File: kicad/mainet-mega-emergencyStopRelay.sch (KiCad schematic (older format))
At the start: 38 parts, among them J38 Screw_Terminal_01x01, J39 Screw_Terminal_01x01, J41 Screw_Terminal_01x01, J43 Screw_Terminal_01x01, J45 Screw_Terminal_01x01, J46 Screw_Terminal_01x01, J47 Screw_Terminal_01x01, J48 Screw_Terminal_01x01, J49 Screw_Terminal_01x01, J50 Screw_Terminal_01x01, J51 Screw_Terminal_01x01, J52 Screw_Terminal_01x01, J53 Screw_Terminal_01x01, J54 Screw_Terminal_01x01, J55 Screw_Terminal_01x01, J56 Screw_Terminal_01x01, J57 Screw_Terminal_01x01, J58 Screw_Terminal_01x01, J59 Screw_Terminal_01x01, J60 Screw_Terminal_01x01, J61 Screw_Terminal_01x01, J62 Screw_Terminal_01x01, J63 Screw_Terminal_01x01, K10 Contactor-3-poles, K9 relay-4p2t, SW5 emergencyStop, T1 Transformer_2P_1S, U11 socket-4p2t

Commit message: KICAD: Actualizar archivos sch
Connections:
- net labels added: GNDREF
- net labels removed: GNDA
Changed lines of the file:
@@
-$EndComp
-$Comp
-L power:GNDA #PWR039
-U 1 1 5FDC5B2D
-P 750 7300
-F 0 "#PWR039" H 750 7050 50  0001 C CNN
-F 1 "GNDA" H 755 7127 50  0000 C CNN
-F 2 "" H 750 7300 50  0001 C CNN
-F 3 "" H 750 7300 50  0001 C CNN
-	1    750  7300
-	1    0    0    -1
-$EndComp
-$Comp
-L power:PWR_FLAG #FLG05
-U 1 1 5FDC5C70
-P 3450 5300
-F 0 "#FLG05" H 3450 5375 50  0001 C CNN
-F 1 "PWR_FLAG" H 3450 5473 50  0000 C CNN
-F 2 "" H 3450 5300 50  0001 C CNN
-F 3 "~" H 3450 5300 50  0001 C CNN
-	1    3450 5300
-	1    0    0    -1
 $EndComp
 $Comp
 L power:PWR_FLAG #FLG06
 U 1 1 5FDC5CFA
-P 1200 7300
-F 0 "#FLG06" H 1200 7375 50  0001 C CNN
-F 1 "PWR_FLAG" H 1200 7473 50  0000 C CNN
-F 2 "" H 1200 7300 50  0001 C CNN
-F 3 "~" H 1200 7300 50  0001 C CNN
-	1    1200 7300
+P 1550 6500
+F 0 "#FLG06" H 1550 6575 50  0001 C CNN
+F 1 "PWR_FLAG" H 1550 6673 50  0000 C CNN
+F 2 "" H 1550 6500 50  0001 C CNN
+F 3 "~" H 1550 6500 50  0001 C CNN
+	1    1550 6500
 	1    0    0    1
 $EndComp
 Wire Wire Line
-	750  7300 1200 7300
-$Comp
-L power:GNDA #PWR041
-U 1 1 5FDC9687
-P 1100 6500
-F 0 "#PWR041" H 1100 6250 50  0001 C CNN
-F 1 "GNDA" H 1105 6327 50  0000 C CNN
-F 2 "" H 1100 6500 50  0001 C CNN
-F 3 "" H 1100 6500 50  0001 C CNN
-	1    1100 6500
-	1    0    0    -1
-$EndComp
+	1100 6500 1550 6500
 Wire Wire Line
 	1100 5300 1100 5700
@@
 Text Label 2850 1700 0    50   ~ 0
 L11
+$Comp
+L power:GNDREF #PWR0108
+U 1 1 60EEEDA8
+P 1100 6500
+F 0 "#PWR0108" H 1100 6250 50  0001 C CNN
+F 1 "GNDREF" H 1105 6327 50  0000 C CNN
+F 2 "" H 1100 6500 50  0001 C CNN
+F 3 "" H 1100 6500 50  0001 C CNN
+	1    1100 6500
+	1    0    0    -1
+$EndComp
+Connection ~ 1100 6500
+$Comp
+L power:PWR_FLAG #FLG0102
+U 1 1 60F2B4A9
+P 3450 5300
+F 0 "#FLG0102" H 3450 5375 50  0001 C CNN
+F 1 "PWR_FLAG" H 3450 5473 50  0000 C CNN
+F 2 "" H 3450 5300 50  0001 C CNN
+F 3 "~" H 3450 5300 50  0001 C CNN
+	1    3450 5300
+	1    0    0    -1
+$EndComp
 $EndSCHEMATC

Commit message: KICAD: Actualizar .sch regleta de conexiones
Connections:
- net L5 is gone; now on net L4: F5.2, T1.3 (H3)
- net 5 renamed Neutro
- net L11 renamed 120VAC
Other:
- moved on the sheet: F14, F4, F5, F6, FU1, FU2, FU3, FU7, FU8, FU9, J38, J39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

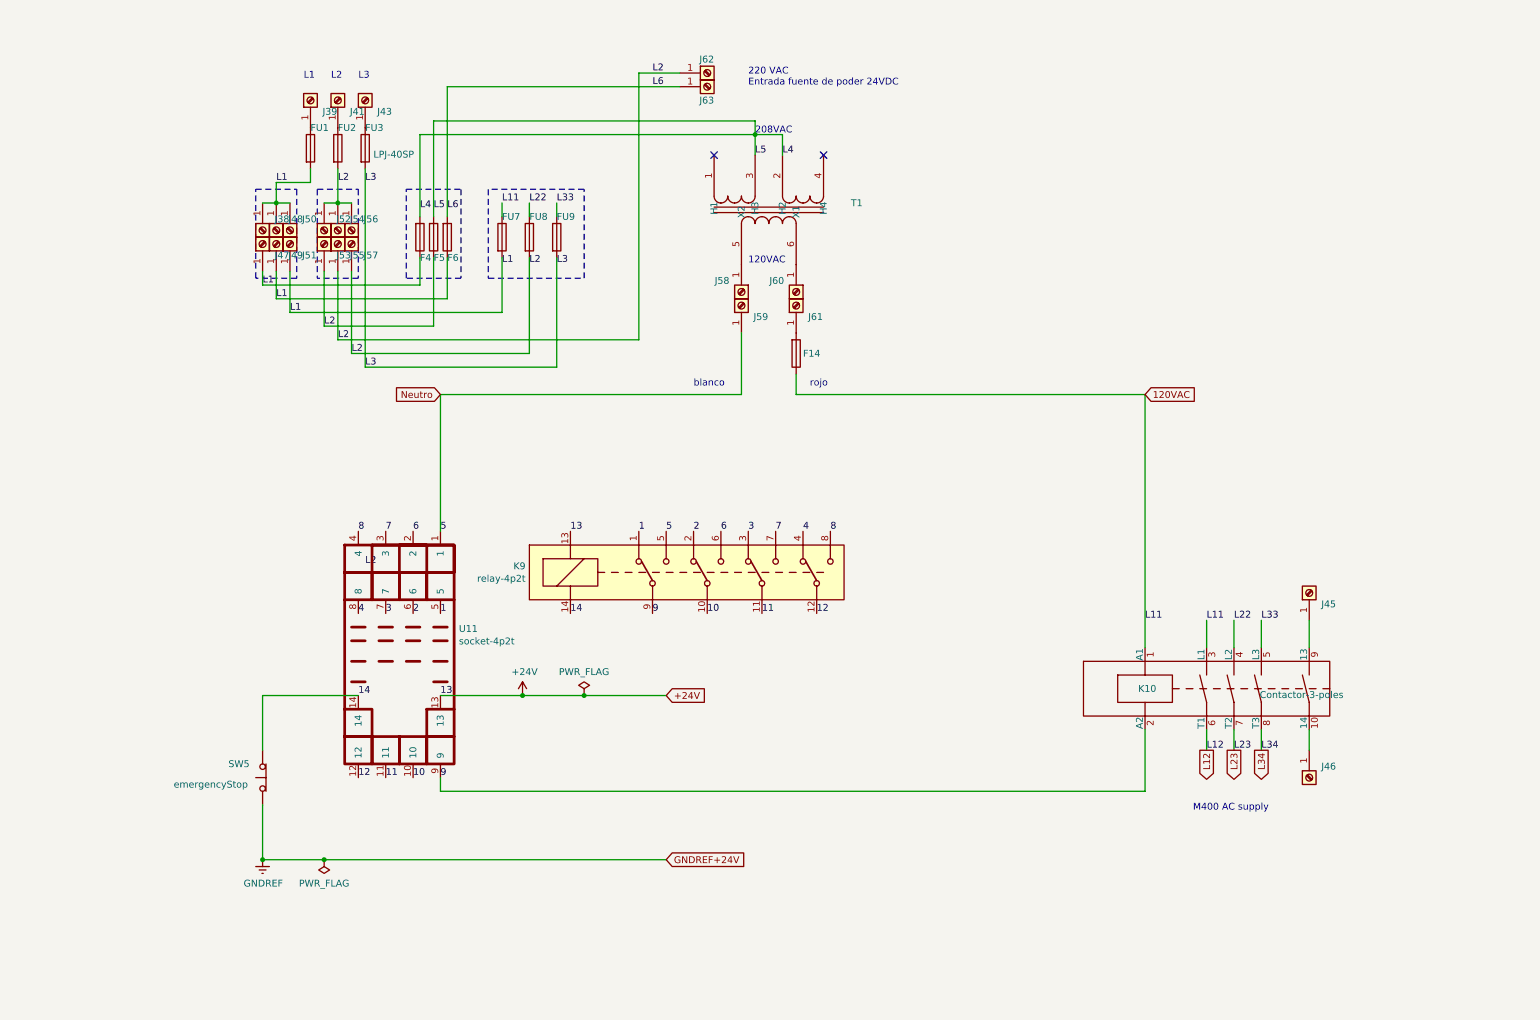
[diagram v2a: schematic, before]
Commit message: KICAD: Actualizar sch del pulsador de emergencia
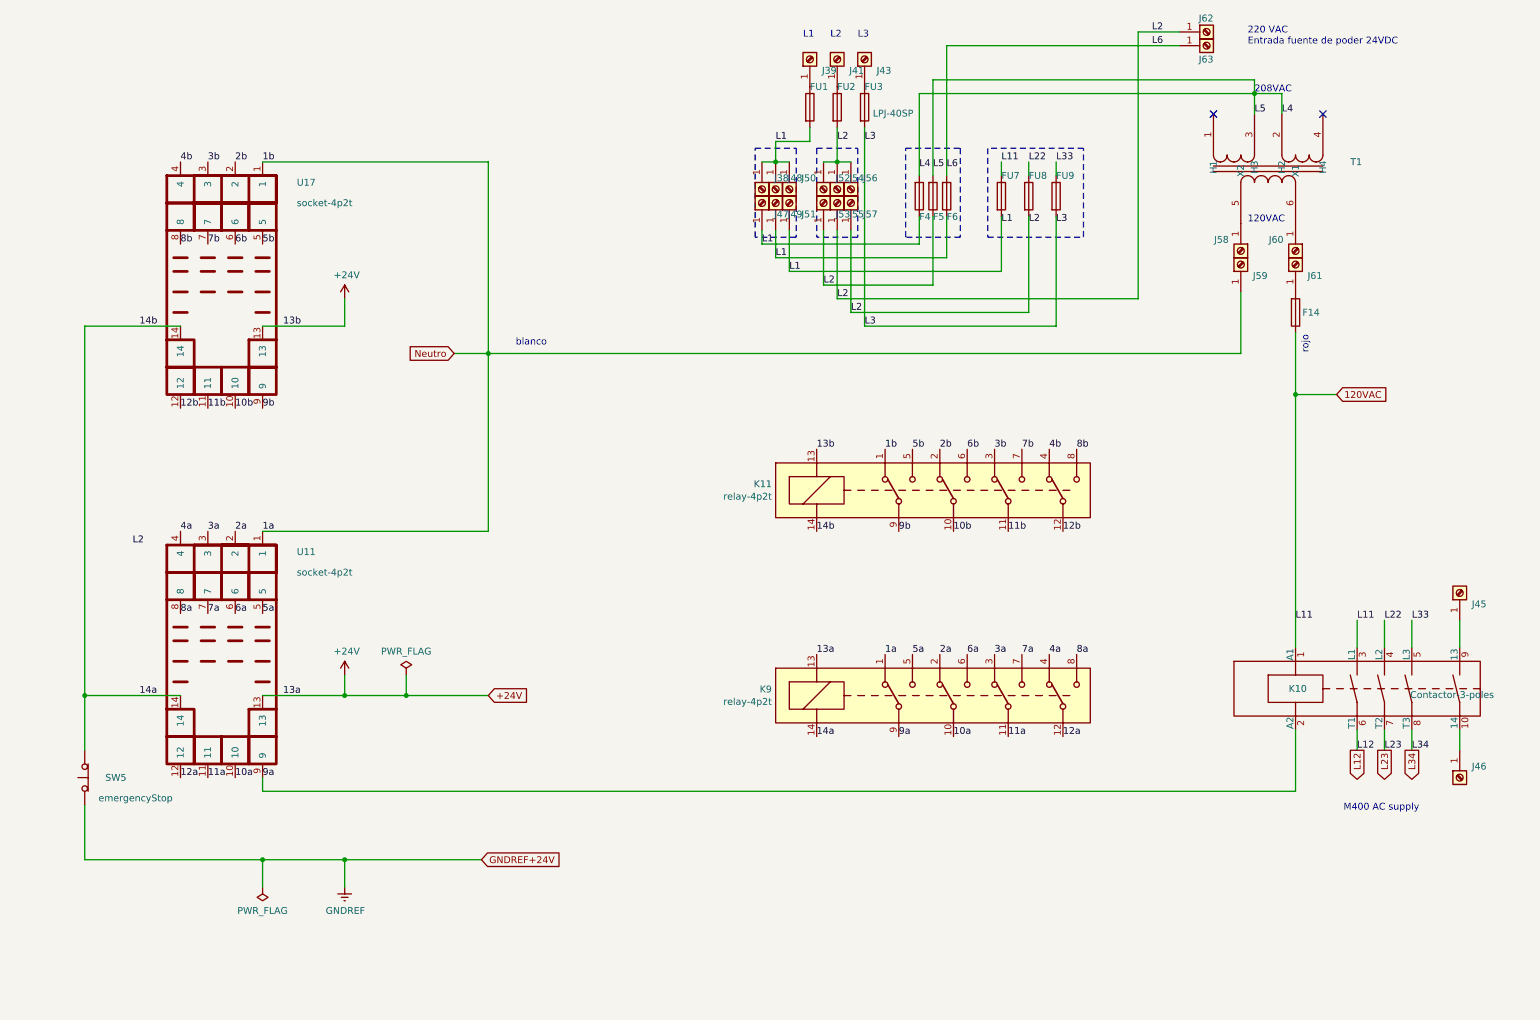
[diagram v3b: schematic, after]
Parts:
- added K11: relay-4p2t, symbol mainet-mega-rescue:relay-4p2t-ng-relays
- added U17: socket-4p2t, symbol mainet-mega-rescue:socket-4p2t-ng-relays
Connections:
- net +24V: now also K11.13 (+), U17.13
- net Neutro: now also K9.1 (NC1), K11.1 (NC1), U17.1; no longer K9.5 (NO1)
- net 1 renamed 5a
- net 5a: now also K9.5 (NO1); no longer K9.1 (NC1)
- net 10 renamed 10a
- net 11 renamed 11a
- net 12 renamed 12a
- net 14 renamed 14a
- net 14a: now also K11.14 (-), U17.14
- net 2 renamed 2a
- net 2a: now also U11.2; no longer U11.6
- net 3 renamed 3a
- net 3a: now also U11.3; no longer U11.7
- net 4 renamed 4a
- net 4a: now also U11.4; no longer U11.8
- net 6 renamed 6a
- net 6a: now also U11.6; no longer U11.2
- net 7 renamed 7a
- net 7a: now also U11.7; no longer U11.3
- net 8 renamed 8a
- net 8a: now also U11.8; no longer U11.4
- net 9 renamed 9a
- new net 10b: K11.10 (C2), U17.10
- new net 11b: K11.11 (C3), U17.11
- new net 12b: K11.12 (C4), U17.12
- new net 2b: K11.2 (NC2), U17.2
- new net 3b: K11.3 (NC3), U17.3
- new net 4b: K11.4 (NC4), U17.4
- new net 5b: K11.5 (NO1), U17.5
- new net 6b: K11.6, U17.6
- new net 7b: K11.7 (NO3), U17.7
- new net 8b: K11.8 (NO4), U17.8
- new net 9b: K11.9 (C1), U17.9
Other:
- moved on the sheet: F14, F4, F5, F6, FU1, FU2, FU3, FU7, FU8, FU9, J38, J39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

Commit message: KICAD: Actualizar .sch del relé de parada de emergencia
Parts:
- added J102: Screw_Terminal_01x02, symbol Connector:Screw_Terminal_01x02
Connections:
- net 10b: now also J102.2 (Pin_2)
- net 9b: now also J102.1 (Pin_1)
- net Neutro: no longer K11.1 (NC1), U17.1
- net 2b renamed lowerClutch2+
- net 3b renamed lowerClutch1-
- net 4b renamed lowerClutch1+
- new net lowerClutch2-: K11.1 (NC1), U17.1
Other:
- note added: "Ouput-"
- note added: "Output+"
- note added: "Tarjeta MP2"
- moved on the sheet: K11, K9, U17
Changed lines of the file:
@@
 Sheet 4 22
 Title "Mainet-mega -- Diagrama Alimentación AC"
-Date "2021-07-15"
+Date "2021-07-16"
 Rev "1.0"
 Comp "Tovenca"
@@
 L mainet-mega-rescue:relay-4p2t-ng-relays K9
 U 1 1 5FE04F1A
-P 6950 5600
+P 4200 4900
 AR Path="/5FE04F1A" Ref="K9"  Part="1"
 AR Path="/5FF9030A/5FE04F1A" Ref="K9"  Part="1"
-F 0 "K9" H 5722 5646 50  0000 R CNN
-F 1 "relay-4p2t" H 5722 5555 50  0000 R CNN
-F 2 "" H 7400 6500 50  0001 C CNN
-F 3 "" H 7400 6500 50  0001 C CNN
-	1    6950 5600
+F 0 "K9" H 2972 4946 50  0000 R CNN
+F 1 "relay-4p2t" H 2972 4855 50  0001 R CNN
+F 2 "" H 4650 5800 50  0001 C CNN
+F 3 "" H 4650 5800 50  0001 C CNN
+	1    4200 4900
 	1    0    0    -1
 $EndComp
@@
 	1    0    0    -1
 $EndComp
-Text Label 1050 4500 0    50   ~ 0
-L2
 Text Label 9550 5050 0    50   ~ 0
 L11
@@
 Wire Wire Line
 	10750 5850 10750 6000
-$Comp
-L mainet-mega-rescue:socket-4p2t-ng-relays U11
-U 1 1 5FDD58E8
-P 1700 5300
-AR Path="/5FDD58E8" Ref="U11"  Part="1"
-AR Path="/5FF9030A/5FDD58E8" Ref="U11"  Part="1"
-F 0 "U11" H 2250 6050 50  0000 L CNN
-F 1 "socket-4p2t" H 2250 5900 50  0000 L CNN
-F 2 "" H 2150 6200 50  0001 C CNN
-F 3 "" H 2150 6200 50  0001 C CNN
-	1    1700 5300
-	1    0    0    -1
-$EndComp
 Text Label 1400 4400 0    50   ~ 0
 4a
@@
 Text Label 2000 4400 0    50   ~ 0
 1a
-Text Label 7950 5300 0    50   ~ 0
+Text Label 5200 4600 0    50   ~ 0
 8a
-Text Label 6750 5300 0    50   ~ 0
+Text Label 4000 4600 0    50   ~ 0
 5a
-Text Label 7150 5300 0    50   ~ 0
+Text Label 4400 4600 0    50   ~ 0
 6a
-Text Label 7550 5300 0    50   ~ 0
+Text Label 4800 4600 0    50   ~ 0
 7a
 Text Label 1400 5000 0    50   ~ 0
@@
 Text Label 2150 5600 0    50   ~ 0
 13a
-Text Label 6950 5300 0    50   ~ 0
+Text Label 4200 4600 0    50   ~ 0
 2a
-Text Label 7350 5300 0    50   ~ 0
+Text Label 4600 4600 0    50   ~ 0
 3a
-Text Label 7750 5300 0    50   ~ 0
+Text Label 5000 4600 0    50   ~ 0
 4a
-Text Label 7050 5900 0    50   ~ 0
+Text Label 4300 5200 0    50   ~ 0
 10a
-Text Label 6650 5900 0    50   ~ 0
+Text Label 3900 5200 0    50   ~ 0
 9a
-Text Label 7450 5900 0    50   ~ 0
+Text Label 4700 5200 0    50   ~ 0
 11a
-Text Label 7850 5900 0    50   ~ 0
+Text Label 5100 5200 0    50   ~ 0
 12a
-Text Label 6550 5300 0    50   ~ 0
+Text Label 3800 4600 0    50   ~ 0
 1a
-Text Label 6050 5300 0    50   ~ 0
+Text Label 3300 4600 0    50   ~ 0
 13a
-Text Label 6050 5900 0    50   ~ 0
+Text Label 3300 5200 0    50   ~ 0
 14a
 Wire Wire Line
@@
 	0    -1   -1   0
 $EndComp
-Wire Wire Line
-	9150 2650 9150 3100
-Text Notes 3850 3050 0    50   ~ 0
+Text Notes 9100 3050 1    50   ~ 0
 blanco
 Text Notes 9650 3100 1    50   ~ 0
@@
 Text GLabel 9850 3400 2    50   Input ~ 0
 120VAC
-Text GLabel 3400 3100 0    50   Input ~ 0
+Text GLabel 8850 3400 0    50   Input ~ 0
 Neutro
 Connection ~ 9250 1200
@@
 L mainet-mega-rescue:socket-4p2t-ng-relays U?
 U 1 1 611478DC
-P 1700 2600
+P 1700 2050
 AR Path="/611478DC" Ref="U?"  Part="1"
 AR Path="/5FF9030A/611478DC" Ref="U17"  Part="1"
-F 0 "U17" H 2250 3350 50  0000 L CNN
-F 1 "socket-4p2t" H 2250 3200 50  0000 L CNN
-F 2 "" H 2150 3500 50  0001 C CNN
-F 3 "" H 2150 3500 50  0001 C CNN
-	1    1700 2600
-	1    0    0    -1
-$EndComp
-Wire Wire Line
-	700  5600 700  2900
-Wire Wire Line
-	700  2900 1400 2900
+F 0 "U17" H 900 2750 50  0000 L CNN
+F 1 "socket-4p2t" H 750 2650 50  0000 L CNN
+F 2 "" H 2150 2950 50  0001 C CNN
+F 3 "" H 2150 2950 50  0001 C CNN
+	1    1700 2050
+	1    0    0    -1
+$EndComp
+Wire Wire Line
+	700  2350 1400 2350
 Connection ~ 700  5600
 $Comp
 L mainet-mega-rescue:relay-4p2t-ng-relays K?
 U 1 1 611801A8
-P 6950 4100
+P 4200 2750
 AR Path="/611801A8" Ref="K?"  Part="1"
 AR Path="/5FF9030A/611801A8" Ref="K11"  Part="1"
-F 0 "K11" H 5722 4146 50  0000 R CNN
-F 1 "relay-4p2t" H 5722 4055 50  0000 R CNN
-F 2 "" H 7400 5000 50  0001 C CNN
-F 3 "" H 7400 5000 50  0001 C CNN
-	1    6950 4100
-	1    0    0    -1
-$EndComp
-Text Label 7950 3800 0    50   ~ 0
+F 0 "K11" H 2972 2796 50  0000 R CNN
+F 1 "relay-4p2t" H 2972 2705 50  0001 R CNN
+F 2 "" H 4650 3650 50  0001 C CNN
+F 3 "" H 4650 3650 50  0001 C CNN
+	1    4200 2750
+	1    0    0    -1
+$EndComp
+Text Label 5200 2450 0    50   ~ 0
 8b
-Text Label 6750 3800 0    50   ~ 0
+Text Label 4000 2450 0    50   ~ 0
 5b
-Text Label 7150 3800 0    50   ~ 0
+Text Label 4400 2450 0    50   ~ 0
 6b
-Text Label 7550 3800 0    50   ~ 0
+Text Label 4800 2450 0    50   ~ 0
 7b
-Text Label 6950 3800 0    50   ~ 0
+Text Label 4200 2450 0    50   ~ 0
 2b
-Text Label 7350 3800 0    50   ~ 0
+Text Label 4600 2450 0    50   ~ 0
 3b
-Text Label 7750 3800 0    50   ~ 0
+Text Label 5000 2450 0    50   ~ 0
 4b
-Text Label 7050 4400 0    50   ~ 0
+Text Label 4300 3050 0    50   ~ 0
 10b
-Text Label 6650 4400 0    50   ~ 0
+Text Label 3900 3050 0    50   ~ 0
 9b
-Text Label 7850 4400 0    50   ~ 0
+Text Label 5100 3050 0    50   ~ 0
 12b
-Text Label 6550 3800 0    50   ~ 0
+Text Label 3800 2450 0    50   ~ 0
 1b
-Text Label 6050 3800 0    50   ~ 0
+Text Label 3300 2450 0    50   ~ 0
 13b
-Text Label 6050 4400 0    50   ~ 0
+Text Label 3300 3050 0    50   ~ 0
 14b
 Wire Wire Line
-	9150 3100 3650 3100
-Wire Wire Line
-	3650 3100 3650 1700
-Wire Wire Line
-	3650 1700 2000 1700
-Wire Wire Line
-	2000 4400 3650 4400
-Connection ~ 3650 3100
-Wire Wire Line
-	3400 3100 3650 3100
-Wire Wire Line
 	2000 6300 9550 6300
-Wire Wire Line
-	3650 3100 3650 4400
 Wire Wire Line
 	2600 7000 2600 6800
@@
 	2000 6800 2600 6800
 Wire Wire Line
-	2000 2900 2600 2900
-Wire Wire Line
-	2600 2900 2600 2700
+	2000 2350 2600 2350
+Wire Wire Line
+	2600 2350 2600 2150
 $Comp
 L power:+24V #PWR050
 U 1 1 6120B21B
-P 2600 2700
-F 0 "#PWR050" H 2600 2550 50  0001 C CNN
-F 1 "+24V" H 2615 2873 50  0000 C CNN
-F 2 "" H 2600 2700 50  0001 C CNN
-F 3 "" H 2600 2700 50  0001 C CNN
-	1    2600 2700
+P 2600 2150
+F 0 "#PWR050" H 2600 2000 50  0001 C CNN
+F 1 "+24V" H 2615 2323 50  0000 C CNN
+F 2 "" H 2600 2150 50  0001 C CNN
+F 3 "" H 2600 2150 50  0001 C CNN
+	1    2600 2150
 	1    0    0    -1
 $EndComp
@@
 Wire Wire Line
 	3050 5450 3050 5600
-Text Label 7450 4400 0    50   ~ 0
+Text Label 4700 3050 0    50   ~ 0
 11b
-Text Label 2150 2900 0    50   ~ 0
+Text Label 2150 2350 0    50   ~ 0
 13b
-Text Label 1100 2900 0    50   ~ 0
+Text Label 1100 2350 0    50   ~ 0
 14b
-Text Label 2000 3500 0    50   ~ 0
+Text Label 2000 2950 0    50   ~ 0
 9b
-Text Label 1800 3500 0    50   ~ 0
+Text Label 1800 2950 0    50   ~ 0
 10b
-Text Label 1600 3500 0    50   ~ 0
+Text Label 1600 2950 0    50   ~ 0
 11b
-Text Label 1400 3500 0    50   ~ 0
+Text Label 1400 2950 0    50   ~ 0
 12b
-Text Label 1400 2300 0    50   ~ 0
+Text Label 1400 1750 0    50   ~ 0
 8b
-Text Label 1600 2300 0    50   ~ 0
+Text Label 1600 1750 0    50   ~ 0
 7b
-Text Label 1800 2300 0    50   ~ 0
+Text Label 1800 1750 0    50   ~ 0
 6b
-Text Label 2000 2300 0    50   ~ 0
+Text Label 2000 1750 0    50   ~ 0
 5b
-Text Label 1400 1700 0    50   ~ 0
+Text Label 1400 1150 0    50   ~ 0
 4b
-Text Label 1600 1700 0    50   ~ 0
+Text Label 1600 1150 0    50   ~ 0
 3b
-Text Label 1800 1700 0    50   ~ 0
+Text Label 1800 1150 0    50   ~ 0
 2b
-Text Label 2000 1700 0    50   ~ 0
+Text Label 2000 1150 0    50   ~ 0
 1b
+Text Notes 3700 3800 0    50   ~ 0
+Tarjeta MP2
+Wire Notes Line
+	3200 3400 4200 3400
+$Comp
+L Connector:Screw_Terminal_01x02 J?
+U 1 1 60F63F1D
+P 3150 3550
+AR Path="/60D1F41B/60F63F1D" Ref="J?"  Part="1"
+AR Path="/5FF9030A/60F63F1D" Ref="J102"  Part="1"
+F 0 "J102" H 3050 3700 50  0000 C CNN
+F 1 "Screw_Terminal_01x02" H 3068 3316 50  0001 C CNN
+F 2 "" H 3150 3550 50  0001 C CNN
+F 3 "~" H 3150 3550 50  0001 C CNN
+	1    3150 3550
+	1    0    0    -1
+$EndComp
+$Comp
+L mainet-mega-rescue:socket-4p2t-ng-relays U11
+U 1 1 5FDD58E8
+P 1700 5300
+AR Path="/5FDD58E8" Ref="U11"  Part="1"
+AR Path="/5FF9030A/5FDD58E8" Ref="U11"  Part="1"
+F 0 "U11" H 900 6000 50  0000 L CNN
+F 1 "socket-4p2t" H 750 5950 50  0000 L CNN
+F 2 "" H 2150 6200 50  0001 C CNN
+F 3 "" H 2150 6200 50  0001 C CNN
+	1    1700 5300
+	1    0    0    -1
+$EndComp
+Wire Wire Line
+	700  2350 700  5600
+Wire Wire Line
+	2000 4400 9150 4400
+Wire Wire Line
+	9150 2650 9150 3400
+Wire Wire Line
+	8850 3400 9150 3400
+Connection ~ 9150 3400
+Wire Wire Line
+	9150 3400 9150 4400
+Wire Notes Line
+	3200 3400 3200 3800
+Wire Notes Line
+	3200 3800 4200 3800
+Wire Notes Line
+	4200 3800 4200 3400
+Wire Wire Line
+	1800 2950 1800 3650
+Wire Wire Line
+	2000 2950 2000 3550
+Text Label 2050 3550 0    50   ~ 0
+lowerClutchControl-
+Text Label 2050 3650 0    50   ~ 0
+lowerClutchControl+
+Wire Wire Line
+	2000 3550 2950 3550
+Wire Wire Line
+	1800 3650 2950 3650
+Text Notes 3250 3550 0    50   ~ 0
+Ouput-
+Text Notes 3250 3700 0    50   ~ 0
+Output+
+Text GLabel 3000 650  2    50   Input ~ 0
+lowerClutch1+
+Text GLabel 3000 750  2    50   Input ~ 0
+lowerClutch1-
+Text GLabel 3000 850  2    50   Input ~ 0
+lowerClutch2+
+Text GLabel 3000 950  2    50   Input ~ 0
+lowerClutch2-
+Wire Wire Line
+	1400 650  3000 650
+Wire Wire Line
+	1400 650  1400 1150
+Wire Wire Line
+	3000 750  1600 750
+Wire Wire Line
+	1600 750  1600 1150
+Wire Wire Line
+	3000 850  1800 850
+Wire Wire Line
+	1800 850  1800 1150
+Wire Wire Line
+	3000 950  2000 950
+Wire Wire Line
+	2000 950  2000 1150
 $EndSCHEMATC
